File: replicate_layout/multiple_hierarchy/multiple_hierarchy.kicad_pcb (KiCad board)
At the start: 2 copper layers, 37 parts, among them J201 LEG_out, J501 LEG_out, J801 LEG_out, Q301 CSD19531KCS, Q302 CSD19531KCS, Q601 CSD19531KCS, Q602 CSD19531KCS, Q901 CSD19531KCS, Q902 CSD19531KCS, U1001 INA240, U101 TMS320F28027DA, U301 IR2181, U401 INA240, U601 IR2181, U701 INA240, U901 IR2181

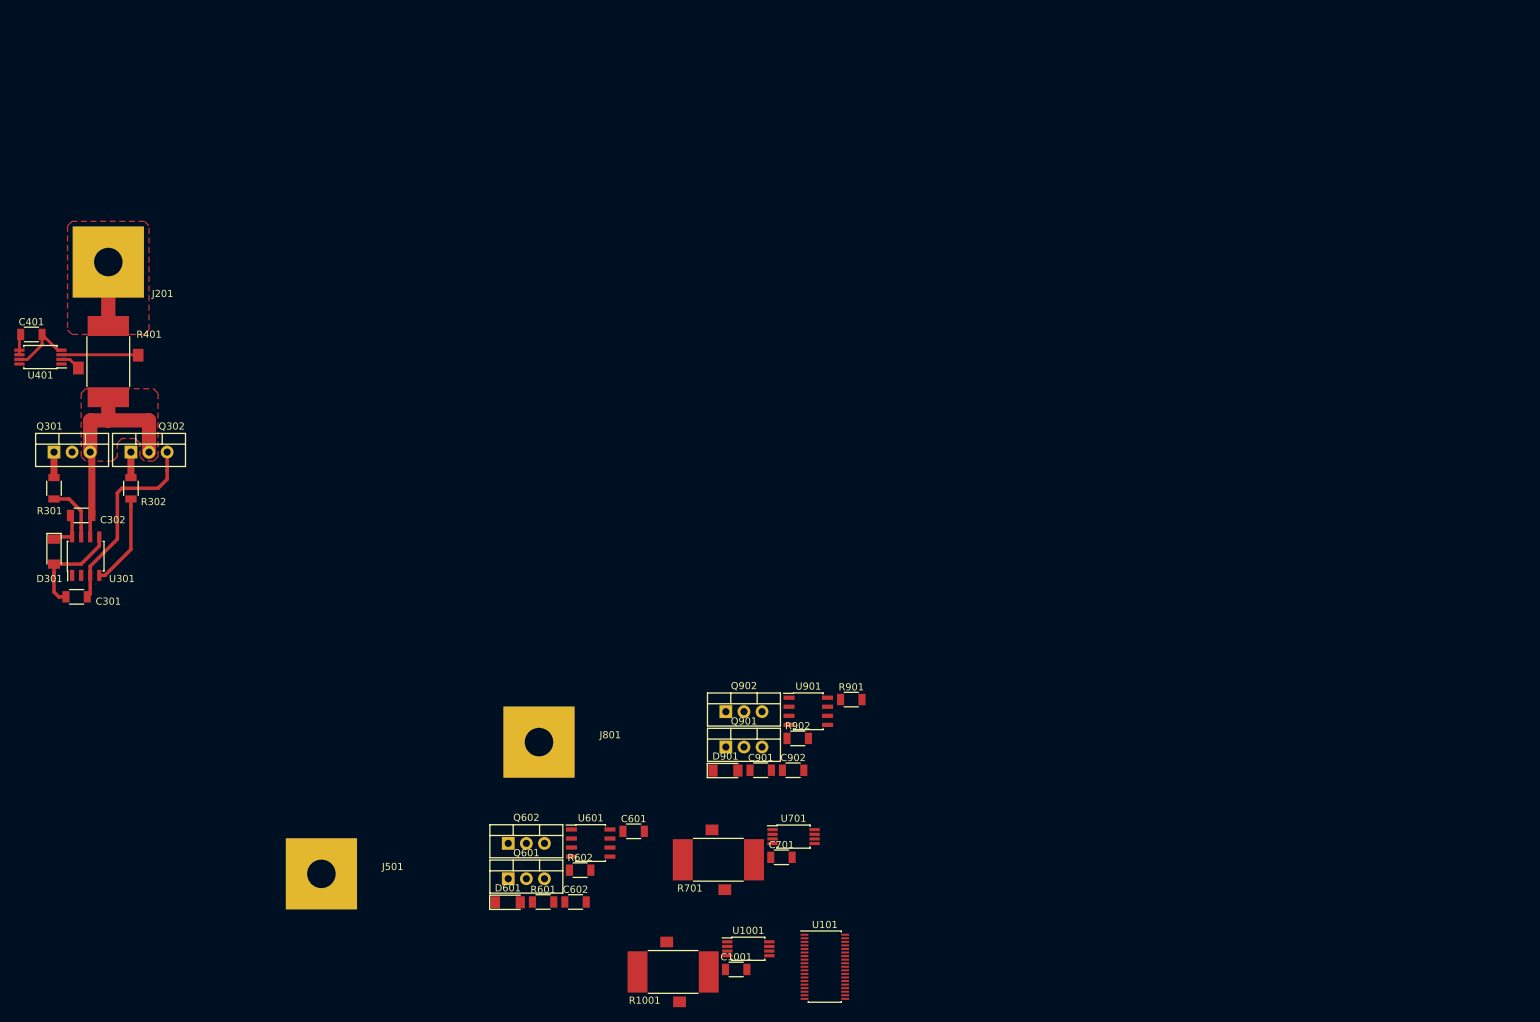
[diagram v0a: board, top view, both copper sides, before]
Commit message: Changed test project to include complex hierarchy
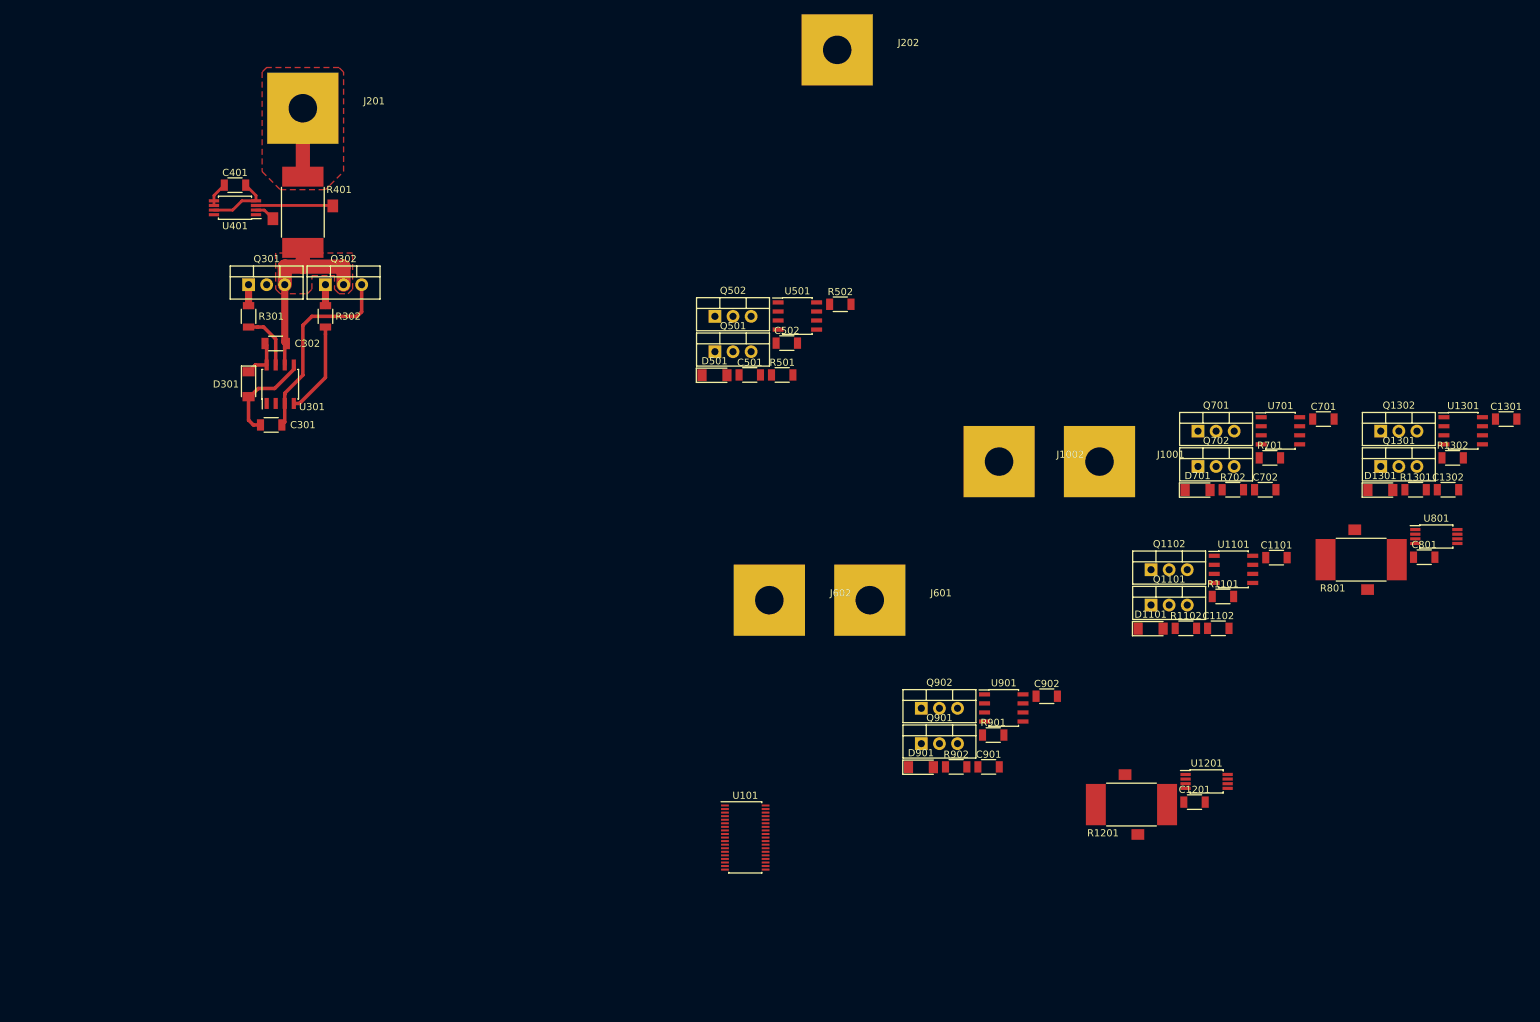
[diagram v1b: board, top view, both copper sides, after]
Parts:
- removed C1001: C1206, Passives:C1206M
- removed C601, C602: 100n, Passives:C1206M
- removed D601: LL4148, Discretes:D_MiniMELF
- removed J501, J801: LEG_out, Connector:Pusa_4mm
- removed Q601, Q602: CSD19531KCS, Discretes:TO-220
- removed R1001: R_Shunt, Passives:RM
- removed R601, R602: 22R, Passives:R1206M
- removed U1001: INA240, Package_SO:TSSOP-8_4.4x3mm_P0.65mm
- removed U601: IR2181, Package_SO:SO8
- added C1101: 100n, Passives:C1206M, F.Cu at (230.0, 91.7)
- added C1102: 100n, Passives:C1206M, F.Cu at (221.8, 101.6)
- added C1201: C1206, Passives:C1206M, F.Cu at (218.5, 126.0)
- added C1301: 100n, Passives:C1206M, F.Cu at (262.2, 72.2)
- added C1302: 100n, Passives:C1206M, F.Cu at (254.1, 82.1)
- added C501: 100n, Passives:C1206M, F.Cu at (156.1, 66.0)
- added C502: 100n, Passives:C1206M, F.Cu at (161.3, 61.5)
- added C702: 100n, Passives:C1206M, F.Cu at (228.4, 82.1)
- added C801: C1206, Passives:C1206M, F.Cu at (250.7, 91.6)
- added D1101: LL4148, Discretes:D_MiniMELF, F.Cu at (212.3, 101.6)
- added D1301: LL4148, Discretes:D_MiniMELF, F.Cu at (244.6, 82.2)
- added D501: LL4148, Discretes:D_MiniMELF, F.Cu at (151.1, 66.1)
- added D701: LL4148, Discretes:D_MiniMELF, F.Cu at (218.9, 82.2)
- added J1001: Pusa_4mm, Connector:Pusa_4mm, F.Cu at (205.2, 78.2)
- added J1002: Pusa_4mm, Connector:Pusa_4mm, F.Cu at (191.1, 78.2)
- added J202: Pusa_4mm, Connector:Pusa_4mm, F.Cu at (168.3, 20.4)
- added J601: Pusa_4mm, Connector:Pusa_4mm, F.Cu at (172.9, 97.6)
- added J602: Pusa_4mm, Connector:Pusa_4mm, F.Cu at (158.8, 97.6)
- added Q1101: CSD19531KCS, Discretes:TO-220, F.Cu at (212.4, 98.3)
- added Q1102: CSD19531KCS, Discretes:TO-220, F.Cu at (212.4, 93.3)
- added Q1301: CSD19531KCS, Discretes:TO-220, F.Cu at (244.6, 78.9)
- added Q1302: CSD19531KCS, Discretes:TO-220, F.Cu at (244.6, 73.9)
- added Q501: CSD19531KCS, Discretes:TO-220, F.Cu at (151.2, 62.7)
- added Q502: CSD19531KCS, Discretes:TO-220, F.Cu at (151.2, 57.8)
- added Q701: CSD19531KCS, Discretes:TO-220, F.Cu at (219.0, 73.9)
- added Q702: CSD19531KCS, Discretes:TO-220, F.Cu at (219.0, 78.9)
- added R1101: 22R, Passives:R1206M, F.Cu at (222.5, 97.1)
- added R1102: 22R, Passives:R1206M, F.Cu at (217.3, 101.6)
- added R1201: R_Shunt, Passives:RM, F.Cu at (209.6, 126.3)
- added R1301: 22R, Passives:R1206M, F.Cu at (249.5, 82.1)
- added R1302: 22R, Passives:R1206M, F.Cu at (254.7, 77.7)
- added R501: 22R, Passives:R1206M, F.Cu at (160.6, 66.0)
- added R502: 22R, Passives:R1206M, F.Cu at (168.8, 56.1)
- added R702: 22R, Passives:R1206M, F.Cu at (223.9, 82.1)
- added R801: R_Shunt, Passives:RM, F.Cu at (241.9, 91.9)
- added U1101: IR2181, Package_SO:SO8, F.Cu at (224.0, 93.3)
- added U1201: INA240, Package_SO:TSSOP-8_4.4x3mm_P0.65mm, F.Cu at (220.2, 123.1)
- added U1301: IR2181, Package_SO:SO8, F.Cu at (256.2, 73.8)
- added U501: IR2181, Package_SO:SO8, F.Cu at (162.8, 57.7)
- added U801: INA240, Package_SO:TSSOP-8_4.4x3mm_P0.65mm, F.Cu at (252.4, 88.7)
- C701: value C1206 -> 100n
- J201: value LEG_out -> Pusa_4mm
- R701: value R_Shunt -> 22R; footprint Passives:RM -> Passives:R1206M
- U701: value INA240 -> IR2181; footprint Package_SO:TSSOP-8_4.4x3mm_P0.65mm -> Package_SO:SO8
- moved C701 97.8 mm to (236.6, 72.2)
- moved R701 95.8 mm to (229.1, 77.7)
- moved U701 89.0 mm to (230.6, 73.8)
- moved C902 37.1 mm to (197.8, 111.1)
- moved C301 36.4 mm to (88.9, 73.0)
- moved R301 36.4 mm to (85.7, 57.8)
- moved R302 36.4 mm to (96.5, 57.8)
- moved C302 36.4 mm to (89.5, 61.6)
- moved U301 36.4 mm to (90.2, 67.3)
- moved D301 36.0 mm to (85.7, 67.3)
- moved Q301 36.0 mm to (85.7, 53.3)
- moved Q302 36.0 mm to (96.5, 53.3)
- moved C401 35.4 mm to (83.8, 39.4)
- moved J201 34.8 mm to (93.3, 28.6)
- moved R401 34.4 mm to (93.3, 43.2)
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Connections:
- net /Leg3/Sensor/IN renamed /Leg2/Power-/OUT
- C701 pad 1: +3V3 -> +15V
- R701 pad 1: /Leg2/Sensor/OUT -> Net-(R701-Pad1)
- R701 pad 2: Net-(R701-Pad2) -> Net-(Q701-Pad1)
- U701 pad 1: Net-(U701-Pad1) -> /Leg2/QH
- U701 pad 2: Net-(R701-Pad3) -> /Leg2/QL
- U701 pad 3: Net-(R701-Pad2) -> -VDC
- U701 pad 4: -VDC -> Net-(R702-Pad1)
- U701 pad 5: +3V3 -> +15V
- U701 pad 6: +3V3 -> /Leg2/Sensor/IN
- U701 pad 7: -VDC -> Net-(R701-Pad1)
- U701 pad 8: /Leg2/Current -> Net-(C702-Pad1)
- U901 pad 1: /Leg3/QH -> /Leg2/QL
- U901 pad 2: /Leg3/QL -> /Leg2/QH
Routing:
- net /Leg1/Sensor/IN: track 32.5 -> 27.4 mm
- net +15V: track 14.6 -> 13.8 mm
- net Net-(Q302-Pad1): track 3.58 -> 2.94 mm
- net Net-(Q301-Pad1): track 3.58 -> 2.94 mm
- net /Leg1/Sensor/OUT: track 8.97 -> 9.61 mm
- net +3V3: track 2.92 -> 3.45 mm

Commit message: Changed test project
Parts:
- moved C502 82.9 mm to (130.2, 138.4)
- moved D501 82.9 mm to (120.0, 142.9)
- moved Q501 82.9 mm to (120.1, 139.6)
- moved Q502 82.9 mm to (120.1, 134.6)
- moved R502 82.9 mm to (137.7, 132.9)
- moved C501 82.9 mm to (125.0, 142.8)
- moved J202 82.9 mm to (137.2, 97.2)
- moved R501 82.9 mm to (129.5, 142.8)
- moved U501 82.9 mm to (131.6, 134.6)
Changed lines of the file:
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@@
   )
   (setup
-    (last_trace_width 0.5)
+    (last_trace_width 0.25)
     (user_trace_width 0.4)
     (user_trace_width 0.5)
@@
   )
   (module Passives:C1206M (layer F.Cu)
-    (at 156.070001 66.010001)
+    (at 124.955001 142.845001)
     (descr "Capacitor SMD 1206, reflow soldering, AVX (see smccp.pdf)")
     (tags "capacitor 1206")
@@
   )
   (module Passives:C1206M (layer F.Cu)
-    (at 161.270001 61.540001)
+    (at 130.155001 138.375001)
     (descr "Capacitor SMD 1206, reflow soldering, AVX (see smccp.pdf)")
     (tags "capacitor 1206")
@@
   )
   (module Discretes:D_MiniMELF (layer F.Cu)
-    (at 151.120001 66.055001)
+    (at 120.005001 142.890001)
     (descr "Diode Mini-MELF")
     (tags "Diode Mini-MELF")
@@
   )
   (module Connector:Pusa_4mm (layer F.Cu)
-    (at 168.340001 20.385001)
+    (at 137.225001 97.220001)
     (fp_text reference J202 (at 10 -1) (layer F.SilkS)
       (effects (font (size 1 1) (thickness 0.15)))
@@
   )
   (module Discretes:TO-220 (layer F.Cu)
-    (at 151.180001 62.745001)
+    (at 120.065001 139.580001)
     (descr "TO-220-3, Vertical, RM 2.54mm")
     (tags "TO-220-3 Vertical RM 2.54mm")
@@
   )
   (module Discretes:TO-220 (layer F.Cu)
-    (at 151.180001 57.785001)
+    (at 120.065001 134.620001)
     (descr "TO-220-3, Vertical, RM 2.54mm")
     (tags "TO-220-3 Vertical RM 2.54mm")
@@
   )
   (module Passives:R1206M (layer F.Cu)
-    (at 160.620001 66.010001)
+    (at 129.505001 142.845001)
     (descr "Capacitor SMD 1206, reflow soldering, AVX (see smccp.pdf)")
     (tags "capacitor 1206")
@@
   )
   (module Passives:R1206M (layer F.Cu)
-    (at 168.780001 56.090001)
+    (at 137.665001 132.925001)
     (descr "Capacitor SMD 1206, reflow soldering, AVX (see smccp.pdf)")
     (tags "capacitor 1206")
@@
   )
   (module Package_SO:SO8 (layer F.Cu)
-    (at 162.750001 57.735001)
+    (at 131.635001 134.570001)
     (descr "8-Lead Plastic Small Outline (SN) - Narrow, 3.90 mm Body [SOIC] (see Microchip Packaging Specification 00000049BS.pdf)")
     (tags "SOIC 1.27")

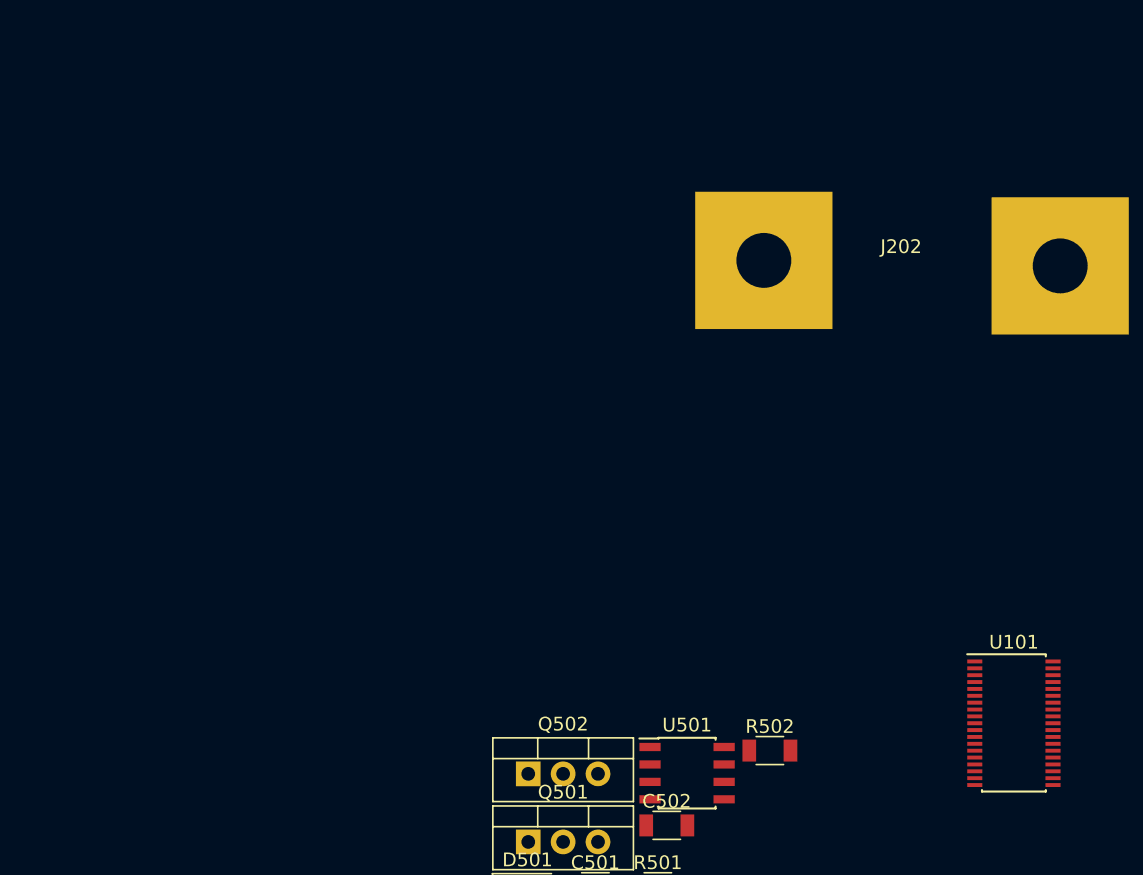
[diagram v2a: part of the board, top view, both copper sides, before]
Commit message: changed test board for better documentation recording
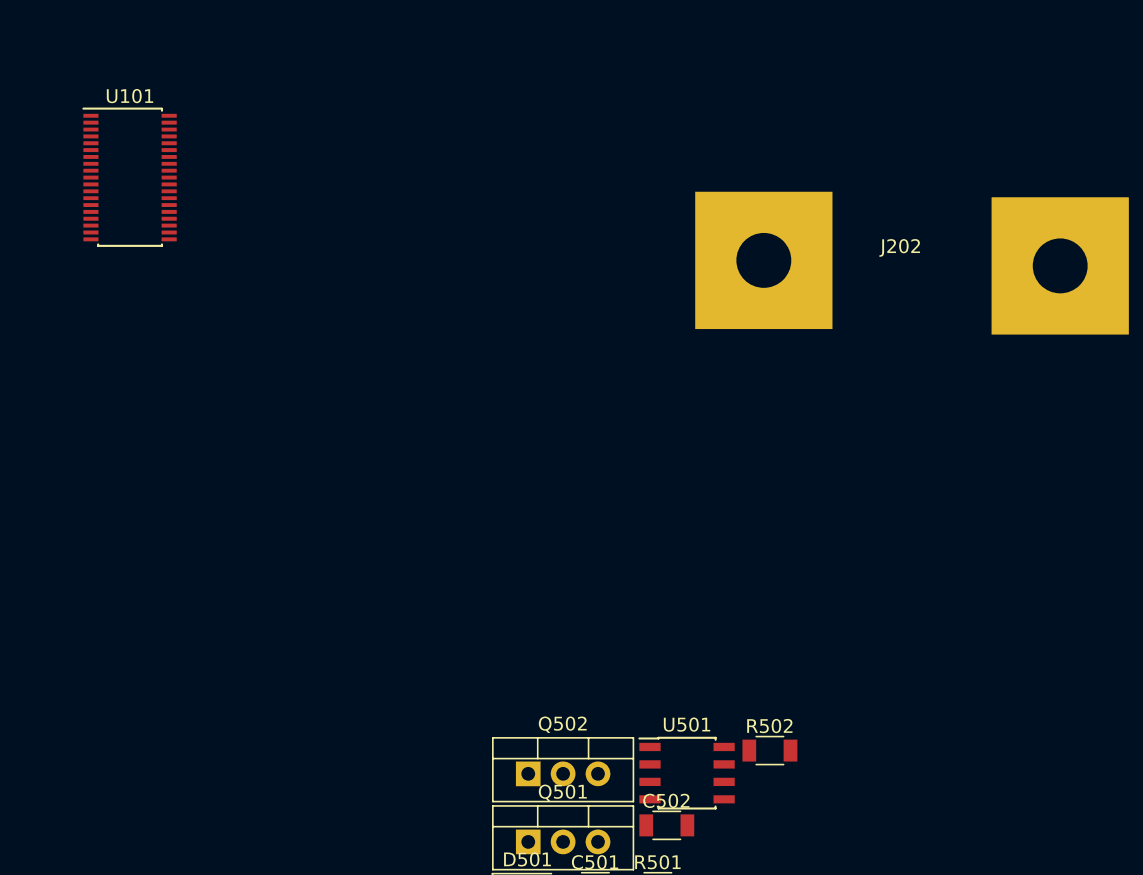
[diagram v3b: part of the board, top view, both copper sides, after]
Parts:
- moved U101 75.7 mm to (91.1, 91.2)
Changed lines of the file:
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@@
   )
   (module Package_SO:TSSOP-38_4.4x9.7mm_P0.5mm (layer F.Cu)
-    (at 155.440001 130.935001)
+    (at 91.059 91.186)
     (descr "TSSOP38: plastic thin shrink small outline package; 38 leads; body width 4.4 mm (see NXP SSOP-TSSOP-VSO-REFLOW.pdf and sot510-1_po.pdf)")
     (tags "SSOP 0.5")
